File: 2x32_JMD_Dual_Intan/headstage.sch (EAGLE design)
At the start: 34 parts, among them U1 RHD2132_QFN, U2 RHD2132_QFN, U3 RHD2132_QFN

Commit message: Finished schematic of 64 chan JMD headstage, started layout.
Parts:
- removed C_A: 0.1uF, resistor:C-USC0402K
- removed C_A1, C_X1, C_Y1, C_Z1: 0.1uF, puggleboard:C_0402
- removed C_REF: 10nF, resistor:C-USC0402K
- removed C_REF1, C_REF2: 10nF, puggleboard:C_0402
- removed C_VDD: 10uF, resistor:C-USC0402K
- removed C_VDD1, C_VDD2: 10uF, puggleboard:C_0603
- removed LED: (no value), resistor:R-EU_R0402
- removed R5, R6: 100, resistor:R-EU_R0402
- removed RLED: 300, resistor:R-EU_R0402
- removed RLED1: 300, puggleboard:R_0402
- removed S2, S4: RHD2000-CABLE-AMP-SIDE, RHD2000:RHD2000-CABLE-AMP-SIDE
- removed S3: OMNETICS_A79025, RHD2000:OMNETICS_A79025
- removed U$2: ADXL335, voigts:ADXL335
- removed U3: RHD2132_QFN, RHD2000:RHD2132_QFN
- added AIN: PINHD-2X35_JMD70, puggleboard:PINHD-2X35_JMD70
- added C1: 0.1uF, puggleboard:C_0402
- added C2, C4: 10nF, puggleboard:C_0402
- added C3, C5: 10uF, puggleboard:C_0603
- C_X, C_Y, C_Z: device resistor:C-USC0402K -> puggleboard:C_0402
- JP1: value (none) -> PINHX-1X5; device puggleboard:PINHD-1X3 -> puggleboard:PINHX-1X5
- R1, R2, R3: device resistor:R-EU_R0402 -> puggleboard:R_0402
- R4: value 100 -> 300; device resistor:R-EU_R0402 -> puggleboard:R_0402
- S1: value OMNETICS_A79025 -> RHD2000-CABLE-AMP-SIDE; device RHD2000:OMNETICS_A79025 -> RHD2000:RHD2000-CABLE-AMP-SIDE
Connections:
- removed net ADC_REF: C_REF.1, U1.ADC_REF
- removed net AUX0UT_B: U3.AUXOUT
- removed net CS+: R1.2, S2.!CS!+, U1.!CS!+
- removed net CS-: R1.1, S2.!CS!-, U1.!CS!-
- removed net LEDOUT: LED.1, RLED.2
- removed net MISO1+: S2.MISO1+, U1.MISO+
- removed net MISO1-: S2.MISO1-, U1.MISO-
- removed net MOSI+: R3.2, S2.MOSI+, U1.MOSI+
- removed net MOSI-: R3.1, S2.MOSI-, U1.MOSI-
- removed net SCLK+: R2.2, S2.SCLK+, U1.SCLK+
- removed net SCLK-: R2.1, S2.SCLK-, U1.SCLK-
- removed net XOUT: C_X.2, U$1.XOUT, U1.AUXIN1
- removed net YOUT: C_Y.2, U$1.YOUT, U1.AUXIN2
- removed net ZOUT: C_Z.2, U$1.ZOUT, U1.AUXIN3
- new net AUXOUT_B: JP1.5, U2.AUXOUT
- new net N$3: C4.1, U2.ADC_REF
- new net N$7: C2.1, U1.ADC_REF
- net AUXOUT_A: now also JP1.4; no longer U2.AUXOUT
- net CS+1: now also R1.2, S1.!CS!+, U1.!CS!+; no longer R4.2, S4.!CS!+, U3.!CS!+
- net CS-1: now also R1.1, S1.!CS!-, U1.!CS!-; no longer R4.1, S4.!CS!-, U3.!CS!-
- net GND: now also C1.2, C2.2, C3.1, C4.2, C5.1, R4.1, S1.VDD; no longer C_A.2, C_A1.2, C_REF.2, C_REF1.1, C_REF1.2, C_REF2.1, C_REF2.2, C_VDD.1, C_VDD1.1, C_VDD2.1, C_X1.1, C_Y1.1, C_Z1.1, RLED.1, RLED1.1, S1.B1, S1.T18, S2.GND, S3.B1, S3.T18, S4.VDD, U$2.COM1, U$2.COM2, U$2.COM3, U$2.COM4, U$2.ST, U2.ADC_REF, U3.ADC_REF, U3.CTR, U3.ELEC_TEST, U3.GND1, U3.GND2, U3.GND3, U3.GND4, U3.VESD
- net IN0: now also AIN.3; no longer S1.B10, S3.B10, U2.IN0
- net IN1: now also AIN.4; no longer S1.B7, S3.B7, U2.IN1
- net IN10: now also AIN.13; no longer S1.T4, S3.T4, U2.IN10
- net IN11: now also AIN.14; no longer S1.T5, S3.T5, U2.IN11
- net IN12: now also AIN.15; no longer S1.T6, S3.T6, U2.IN12
- net IN13: now also AIN.16; no longer S1.T7, S3.T7, U2.IN13
- net IN14: now also AIN.17; no longer S1.T8, S3.T8, U2.IN14
- net IN15: now also AIN.18; no longer S1.T9, S3.T9, U2.IN15
- net IN16: now also AIN.19; no longer S1.T10, S3.T10, U2.IN16
- net IN17: now also AIN.20; no longer S1.T11, S3.T11, U2.IN17
- net IN18: now also AIN.21; no longer S1.T12, S3.T12, U2.IN18
- net IN19: now also AIN.22; no longer S1.T13, S3.T13, U2.IN19
- net IN2: now also AIN.5; no longer S1.B8, S3.B8, U2.IN2
- net IN20: now also AIN.23; no longer S1.T14, S3.T14, U2.IN20
- net IN21: now also AIN.24; no longer S1.T15, S3.T15, U2.IN21
- net IN22: now also AIN.25; no longer S1.T16, S3.T16, U2.IN22
- net IN23: now also AIN.26; no longer S1.T17, S3.T17, U2.IN23
- net IN24: now also AIN.27; no longer S1.B16, S3.B16, U2.IN24
- net IN25: now also AIN.28; no longer S1.B17, S3.B17, U2.IN25
- net IN26: now also AIN.29; no longer S1.B15, S3.B15, U2.IN26
- net IN27: now also AIN.30; no longer S1.B14, S3.B14, U2.IN27
- net IN28: now also AIN.31; no longer S1.B13, S3.B13, U2.IN28
- net IN29: now also AIN.32; no longer S1.B12, S3.B12, U2.IN29
- net IN3: now also AIN.6; no longer S1.B5, S3.B5, U2.IN3
- net IN30: now also AIN.33; no longer S1.B11, S3.B11, U2.IN30
- net IN31: now also AIN.34; no longer S1.B9, S3.B9, U2.IN31
- net IN32: now also AIN.37, U2.IN0; no longer U3.IN0
- net IN33: now also AIN.38, U2.IN1; no longer U3.IN1
- net IN34: now also AIN.39, U2.IN2; no longer U3.IN2
- net IN35: now also AIN.40, U2.IN3; no longer U3.IN3
- net IN36: now also AIN.41, U2.IN4; no longer U3.IN4
- net IN37: now also AIN.42, U2.IN5; no longer U3.IN5
- net IN38: now also AIN.43, U2.IN6; no longer U3.IN6
- net IN39: now also AIN.44, U2.IN7; no longer U3.IN7
- net IN4: now also AIN.7; no longer S1.B6, S3.B6, U2.IN4
- net IN40: now also AIN.45, U2.IN8; no longer U3.IN8
- net IN41: now also AIN.46, U2.IN9; no longer U3.IN9
- net IN42: now also AIN.47, U2.IN10; no longer U3.IN10
- net IN43: now also AIN.48, U2.IN11; no longer U3.IN11
- net IN44: now also AIN.49, U2.IN12; no longer U3.IN12
- net IN45: now also AIN.50, U2.IN13; no longer U3.IN13
- net IN46: now also AIN.51, U2.IN14; no longer U3.IN14
- net IN47: now also AIN.52, U2.IN15; no longer U3.IN15
- net IN48: now also AIN.53, U2.IN16; no longer U3.IN16
- net IN49: now also AIN.54, U2.IN17; no longer U3.IN17
- net IN5: now also AIN.8; no longer S1.B3, S3.B3, U2.IN5
- net IN50: now also AIN.55, U2.IN18; no longer U3.IN18
- net IN51: now also AIN.56, U2.IN19; no longer U3.IN19
- net IN52: now also AIN.57, U2.IN20; no longer U3.IN20
- net IN53: now also AIN.58, U2.IN21; no longer U3.IN21
- net IN54: now also AIN.59, U2.IN22; no longer U3.IN22
- net IN55: now also AIN.60, U2.IN23; no longer U3.IN23
- net IN56: now also AIN.61, U2.IN24; no longer U3.IN24
- net IN57: now also AIN.62, U2.IN25; no longer U3.IN25
- net IN58: now also AIN.63, U2.IN26; no longer U3.IN26
- net IN59: now also AIN.64, U2.IN27; no longer U3.IN27
- net IN6: now also AIN.9; no longer S1.B4, S3.B4, U2.IN6
- net IN60: now also AIN.65, U2.IN28; no longer U3.IN28
- net IN61: now also AIN.66, U2.IN29; no longer U3.IN29
- net IN62: now also AIN.67, U2.IN30; no longer U3.IN30
- net IN63: now also AIN.68, U2.IN31; no longer U3.IN31
- net IN7: now also AIN.10; no longer S1.B2, S3.B2, U2.IN7
- net IN8: now also AIN.11; no longer S1.T2, S3.T2, U2.IN8
- net IN9: now also AIN.12; no longer S1.T3, S3.T3, U2.IN9
- net LEDOUT1: now also R4.2; no longer RLED1.2
- net MISO1+1: now also S1.MISO1+, U1.MISO+; no longer S4.MISO1+, U2.MISO+
- net MISO1-1: now also S1.MISO1-, U1.MISO-; no longer S4.MISO1-, U2.MISO-
- net MOSI+1: now also R3.2, S1.MOSI+, U1.MOSI+; no longer R6.2, S4.MOSI+, U3.MOSI+
- net MOSI-1: now also R3.1, S1.MOSI-, U1.MOSI-; no longer R6.1, S4.MOSI-, U3.MOSI-
- net N$1: now also S1.MISO2-, U2.MISO-; no longer S4.MISO2-, U3.MISO-
- net N$2: now also S1.MISO2+, U2.MISO+; no longer S4.MISO2+, U3.MISO+
- net N$4: now also U2.AUXIN1; no longer U3.AUXIN1
- net N$5: now also U2.AUXIN2; no longer U3.AUXIN2
- net N$6: now also U2.AUXIN3; no longer U3.AUXIN3
- net REF: no longer S1.B18, S1.T1, S3.B18, S3.T1, U3.REF_ELEC
- net SCLK+1: now also R2.2, S1.SCLK+, U1.SCLK+; no longer R5.2, S4.SCLK+, U3.SCLK+
- net SCLK-1: now also R2.1, S1.SCLK-, U1.SCLK-; no longer R5.1, S4.SCLK-, U3.SCLK-
- net VDD: now also C1.1, C3.2, C5.2, S1.GND; no longer C_A.1, C_A1.1, C_VDD.2, C_VDD1.2, C_VDD2.2, LED.2, S2.VDD, S4.GND, U$2.VS1, U$2.VS2, U3.LVDS_EN, U3.VDD1, U3.VDD2, U3.VDD3
- net XOUT1: now also C_X.2, U$1.XOUT, U1.AUXIN1; no longer C_X1.2, U$2.XOUT, U2.AUXIN1
- net YOUT1: now also C_Y.2, U$1.YOUT, U1.AUXIN2; no longer C_Y1.2, U$2.YOUT, U2.AUXIN2
- net ZOUT1: now also C_Z.2, U$1.ZOUT, U1.AUXIN3; no longer C_Z1.2, U$2.ZOUT, U2.AUXIN3

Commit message: Minor.
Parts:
- JP1: value PINHX-1X5 -> PINHX-1X6; device puggleboard:PINHX-1X5 -> puggleboard:PINHX-1X6
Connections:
- net GND: now also JP1.6
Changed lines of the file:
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@@
 <part name="VDD17" library="supply1" deviceset="VDD" device=""/>
 <part name="PWR" library="puggleboard" deviceset="LED" device="_0603"/>
-<part name="JP1" library="puggleboard" deviceset="PINHX-1X5" device=""/>
+<part name="JP1" library="puggleboard" deviceset="PINHX-1X6" device=""/>
 <part name="AIN" library="puggleboard" deviceset="PINHD-2X35" device="_JMD70"/>
 </parts>
@@
 <pinref part="U2" gate="A" pin="GND3"/>
 <pinref part="GND32" gate="1" pin="GND"/>
-<wire x1="231.14" y1="129.54" x2="231.14" y2="119.38" width="0.1524" layer="91"/>
+<wire x1="231.14" y1="129.54" x2="231.14" y2="121.92" width="0.1524" layer="91"/>
+<pinref part="JP1" gate="G$1" pin="6"/>
+<wire x1="231.14" y1="121.92" x2="231.14" y2="119.38" width="0.1524" layer="91"/>
+<wire x1="231.14" y1="121.92" x2="223.52" y2="121.92" width="0.1524" layer="91"/>
+<wire x1="223.52" y1="121.92" x2="223.52" y2="104.14" width="0.1524" layer="91"/>
+<junction x="231.14" y="121.92"/>
 </segment>
 </net>

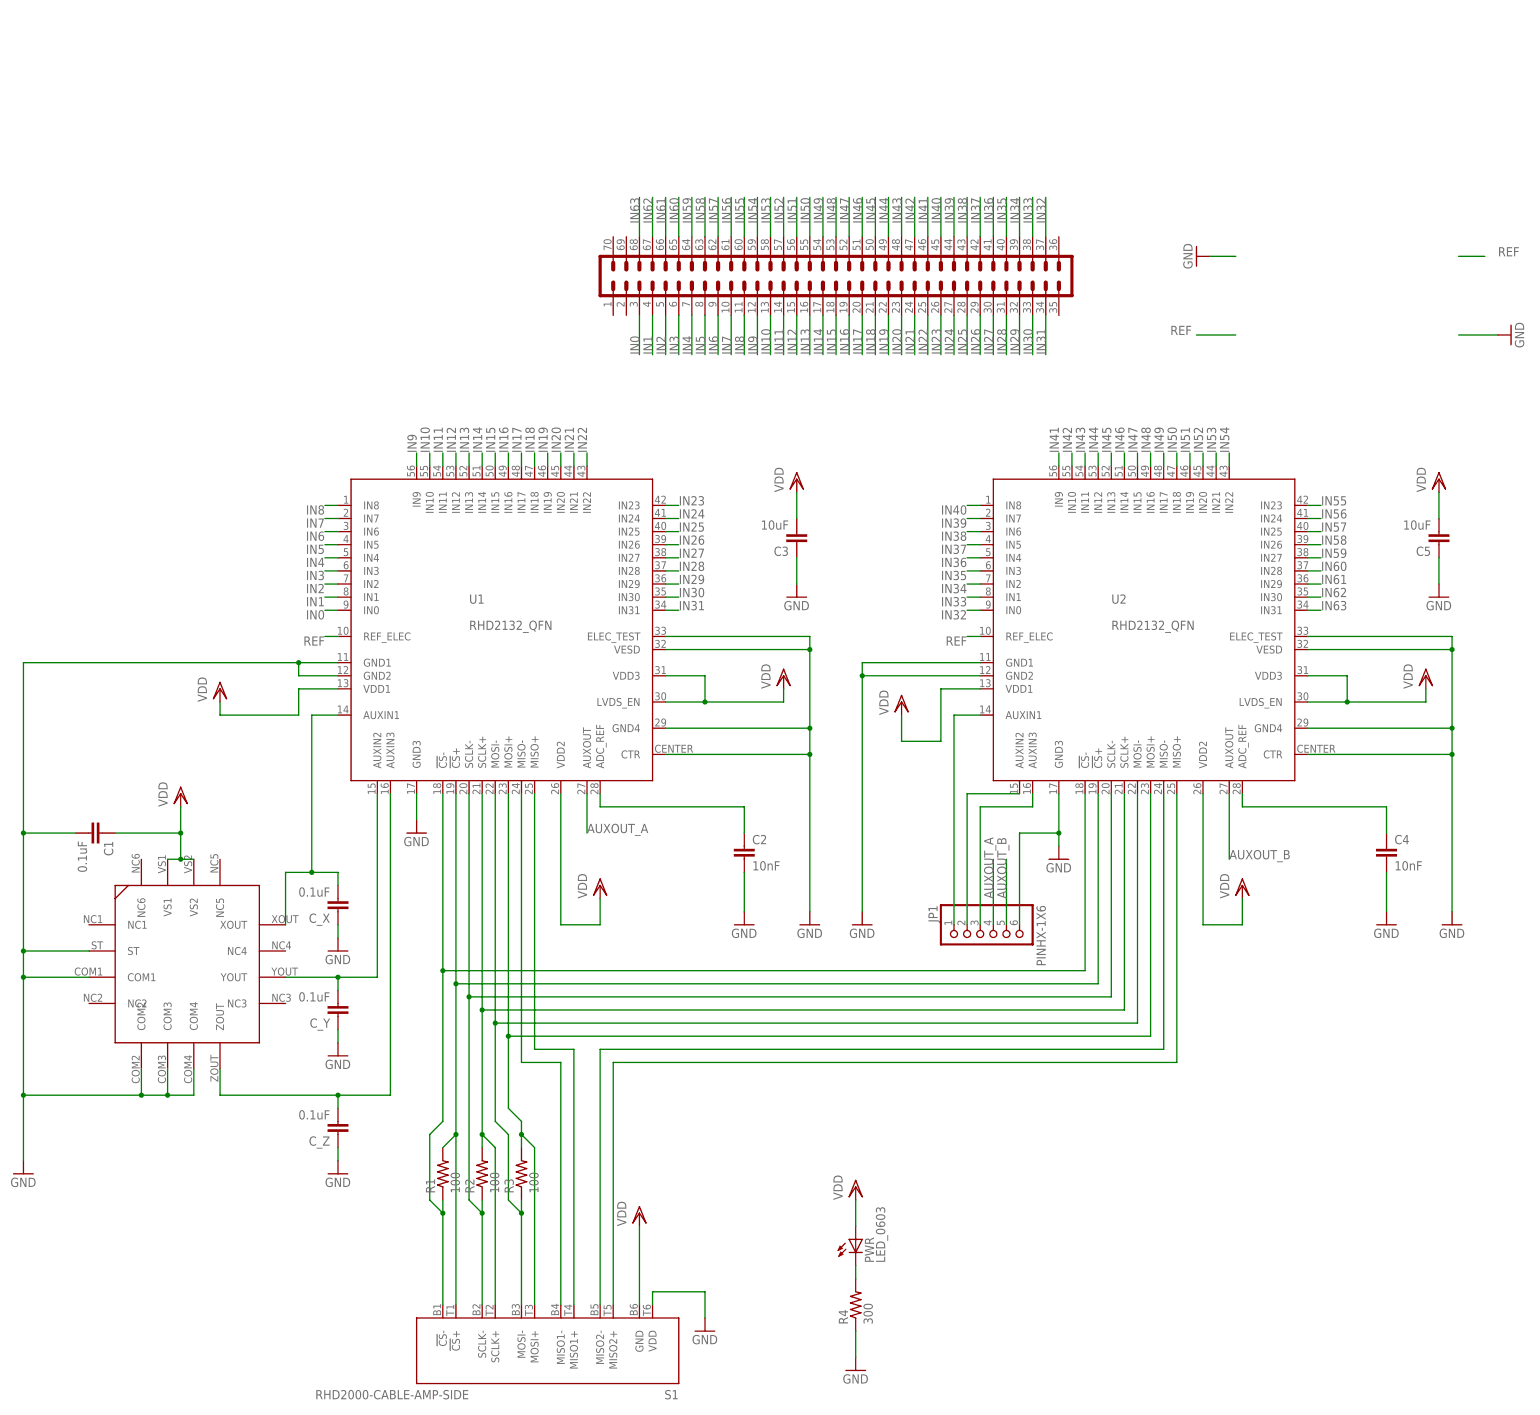
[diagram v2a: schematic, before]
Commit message: Finished initial layout for the 64 channel headstage. I will also make cable interface board. This will be an optional component useful for linking two 64 channel headstages to get 128 with head tracking etc.
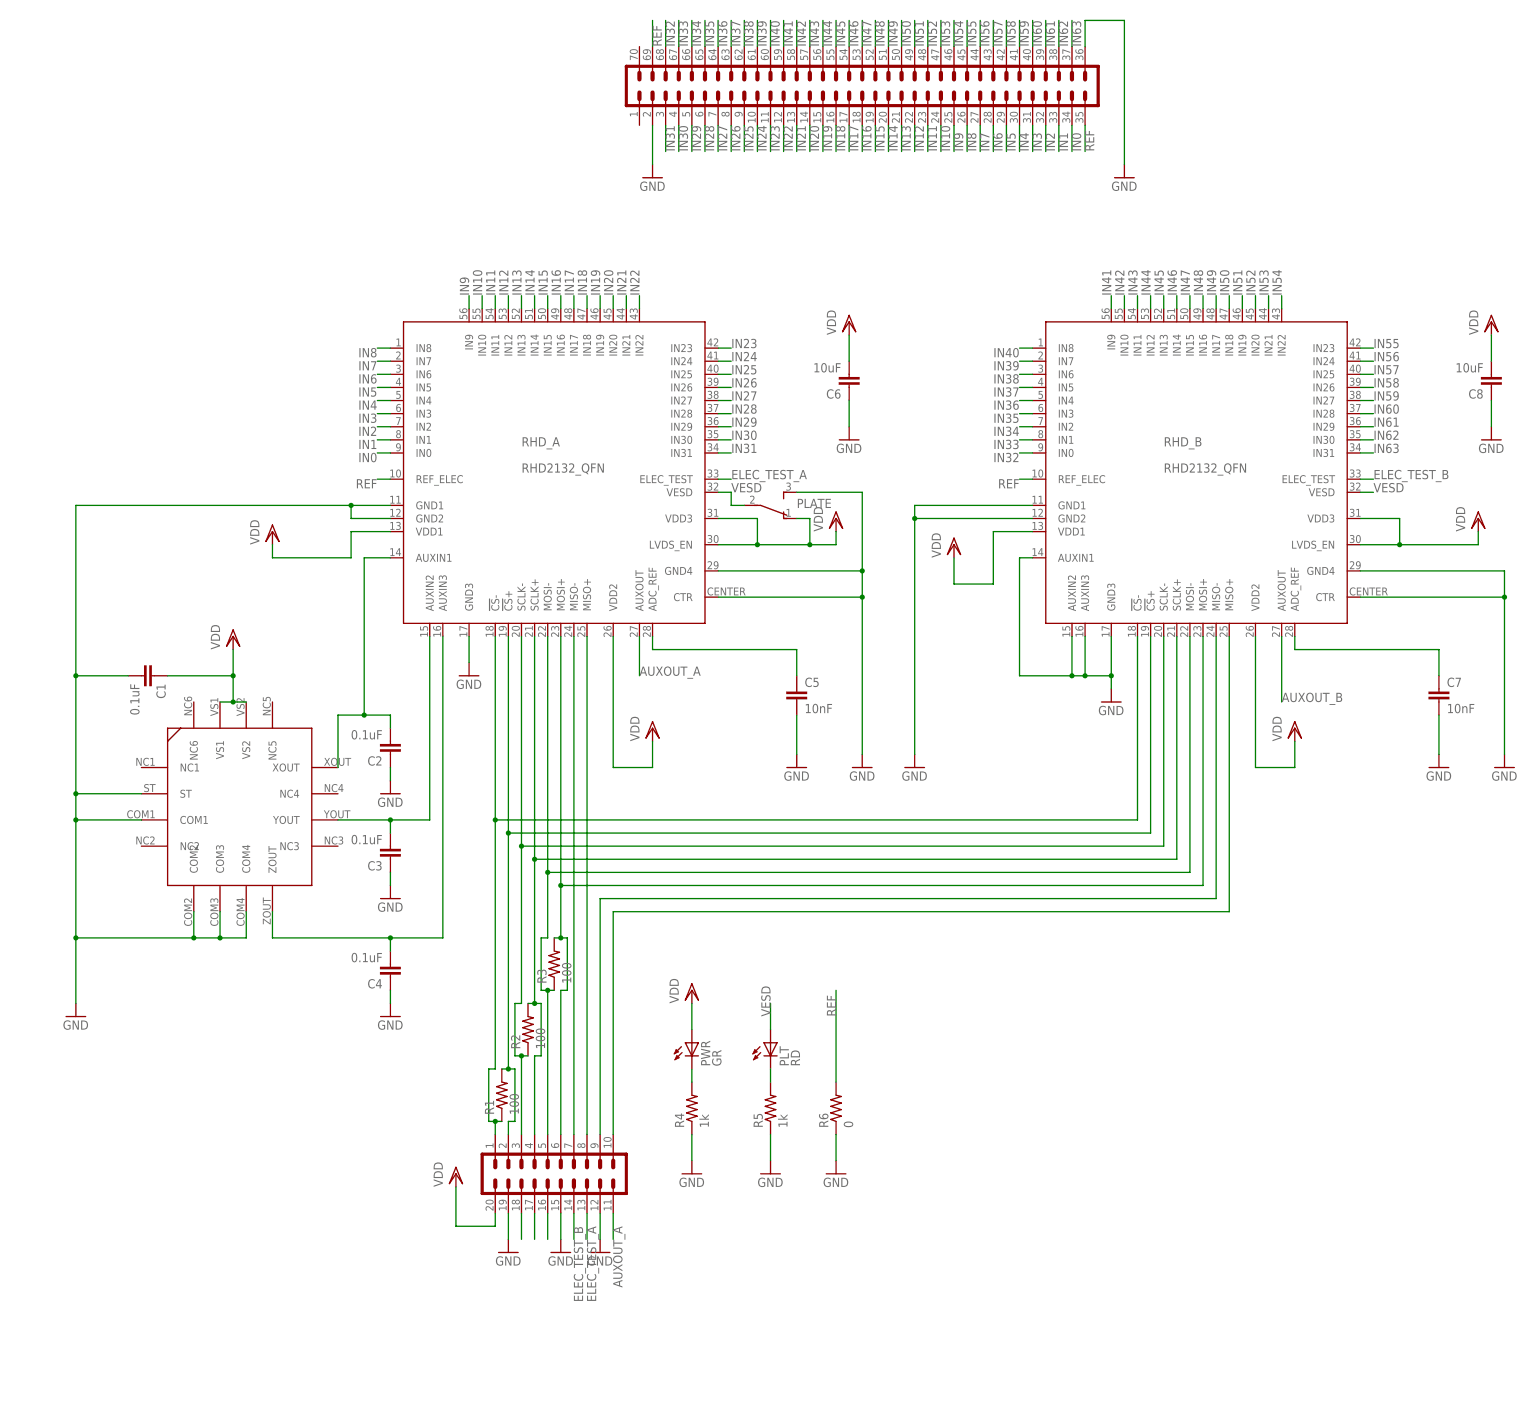
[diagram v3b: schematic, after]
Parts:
- removed C_X, C_Y, C_Z: 0.1uF, puggleboard:C_0402
- removed JP1: PINHX-1X6, puggleboard:PINHX-1X6
- removed S1: RHD2000-CABLE-AMP-SIDE, RHD2000:RHD2000-CABLE-AMP-SIDE
- removed U1, U2: RHD2132_QFN, RHD2000:RHD2132_QFN
- added C6, C8: 10uF, headstage:C_0603
- added C7: 10nF, headstage:C_0402
- added OUT: JMD, headstage:PINHD-2X10_JMD
- added PLATE: (no value), headstage:SPDT_PCM12
- added PLT: RD, puggleboard:LED_0603
- added R5: 1k, headstage:R_0402
- added R6: 0, headstage:R_0402
- added RHD_A, RHD_B: RHD2132_QFN, headstage:RHD2132_QFN
- AIN: value PINHD-2X35_JMD70 -> JMD70; device puggleboard:PINHD-2X35_JMD70 -> headstage:PINHD-2X35_JMD70
- C1: device puggleboard:C_0402 -> headstage:C_0402
- C2, C4: value 10nF -> 0.1uF; device puggleboard:C_0402 -> headstage:C_0402
- C3: value 10uF -> 0.1uF; device puggleboard:C_0603 -> headstage:C_0402
- C5: value 10uF -> 10nF; device puggleboard:C_0603 -> headstage:C_0402
- PWR: value LED_0603 -> GR
- R1, R2, R3: device puggleboard:R_0402 -> headstage:R_0402
- R4: value 300 -> 1k; device puggleboard:R_0402 -> headstage:R_0402
- U$1: device voigts:ADXL335 -> headstage:ADXL335
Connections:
- removed net CS+1: R1.2, S1.!CS!+, U1.!CS!+, U2.!CS!+
- removed net CS-1: R1.1, S1.!CS!-, U1.!CS!-, U2.!CS!-
- removed net MISO1+1: S1.MISO1+, U1.MISO+
- removed net MISO1-1: S1.MISO1-, U1.MISO-
- removed net MOSI+1: R3.2, S1.MOSI+, U1.MOSI+, U2.MOSI+
- removed net MOSI-1: R3.1, S1.MOSI-, U1.MOSI-, U2.MOSI-
- removed net N$1: S1.MISO2-, U2.MISO-
- removed net N$2: S1.MISO2+, U2.MISO+
- removed net N$4: JP1.1, U2.AUXIN1
- removed net N$5: JP1.2, U2.AUXIN2
- removed net N$6: JP1.3, U2.AUXIN3
- removed net SCLK+1: R2.2, S1.SCLK+, U1.SCLK+, U2.SCLK+
- removed net SCLK-1: R2.1, S1.SCLK-, U1.SCLK-, U2.SCLK-
- new net CS+: OUT.2, R1.2, RHD_A.!CS!+, RHD_B.!CS!+
- new net CS-: OUT.1, R1.1, RHD_A.!CS!-, RHD_B.!CS!-
- new net ELEC_TEST_A: OUT.13, RHD_A.ELEC_TEST
- new net ELEC_TEST_B: OUT.14, RHD_B.ELEC_TEST
- new net LEDOUT2: PLT.C, R5.2
- new net MIS02-: OUT.9, RHD_B.MISO-
- new net MISO1+: OUT.8, RHD_A.MISO+
- new net MISO1-: OUT.7, RHD_A.MISO-
- new net MISO2+: OUT.10, RHD_B.MISO+
- new net MOSI+: OUT.6, R3.2, RHD_A.MOSI+, RHD_B.MOSI+
- new net MOSI-: OUT.5, R3.1, RHD_A.MOSI-, RHD_B.MOSI-
- new net N$10: OUT.16
- new net N$8: OUT.18
- new net N$9: OUT.17
- new net SCLK+: OUT.4, R2.2, RHD_A.SCLK+, RHD_B.SCLK+
- new net SCLK-: OUT.3, R2.1, RHD_A.SCLK-, RHD_B.SCLK-
- new net VESD: PLATE.2, PLT.A, RHD_A.VESD, RHD_B.VESD
- net AUXOUT_A: now also OUT.11, RHD_A.AUXOUT; no longer JP1.4, U1.AUXOUT
- net AUXOUT_B: now also RHD_B.AUXOUT; no longer JP1.5, U2.AUXOUT
- net GND: now also AIN.2, AIN.36, C2.1, C4.1, C5.2, C6.1, C7.2, C8.1, OUT.12, OUT.15, OUT.19, PLATE.3, R5.1, R6.1, RHD_A.CTR, RHD_A.GND1, RHD_A.GND2, RHD_A.GND3, RHD_A.GND4, RHD_B.AUXIN1, RHD_B.AUXIN2, RHD_B.AUXIN3, RHD_B.CTR, RHD_B.GND1, RHD_B.GND2, RHD_B.GND3, RHD_B.GND4; no longer C2.2, C4.2, C5.1, C_X.1, C_Y.1, C_Z.1, JP1.6, S1.VDD, U1.CTR, U1.ELEC_TEST, U1.GND1, U1.GND2, U1.GND3, U1.GND4, U1.VESD, U2.CTR, U2.ELEC_TEST, U2.GND1, U2.GND2, U2.GND3, U2.GND4, U2.VESD
- net IN0: now also AIN.34, RHD_A.IN0; no longer AIN.3, U1.IN0
- net IN1: now also AIN.33, RHD_A.IN1; no longer AIN.4, U1.IN1
- net IN10: now also AIN.24, RHD_A.IN10; no longer AIN.13, U1.IN10
- net IN11: now also AIN.23, RHD_A.IN11; no longer AIN.14, U1.IN11
- net IN12: now also AIN.22, RHD_A.IN12; no longer AIN.15, U1.IN12
- net IN13: now also AIN.21, RHD_A.IN13; no longer AIN.16, U1.IN13
- net IN14: now also AIN.20, RHD_A.IN14; no longer AIN.17, U1.IN14
- net IN15: now also AIN.19, RHD_A.IN15; no longer AIN.18, U1.IN15
- net IN16: now also AIN.18, RHD_A.IN16; no longer AIN.19, U1.IN16
- net IN17: now also AIN.17, RHD_A.IN17; no longer AIN.20, U1.IN17
- net IN18: now also AIN.16, RHD_A.IN18; no longer AIN.21, U1.IN18
- net IN19: now also AIN.15, RHD_A.IN19; no longer AIN.22, U1.IN19
- net IN2: now also AIN.32, RHD_A.IN2; no longer AIN.5, U1.IN2
- net IN20: now also AIN.14, RHD_A.IN20; no longer AIN.23, U1.IN20
- net IN21: now also AIN.13, RHD_A.IN21; no longer AIN.24, U1.IN21
- net IN22: now also AIN.12, RHD_A.IN22; no longer AIN.25, U1.IN22
- net IN23: now also AIN.11, RHD_A.IN23; no longer AIN.26, U1.IN23
- net IN24: now also AIN.10, RHD_A.IN24; no longer AIN.27, U1.IN24
- net IN25: now also AIN.9, RHD_A.IN25; no longer AIN.28, U1.IN25
- net IN26: now also AIN.8, RHD_A.IN26; no longer AIN.29, U1.IN26
- net IN27: now also AIN.7, RHD_A.IN27; no longer AIN.30, U1.IN27
- net IN28: now also AIN.6, RHD_A.IN28; no longer AIN.31, U1.IN28
- net IN29: now also AIN.5, RHD_A.IN29; no longer AIN.32, U1.IN29
- net IN3: now also AIN.31, RHD_A.IN3; no longer AIN.6, U1.IN3
- net IN30: now also AIN.4, RHD_A.IN30; no longer AIN.33, U1.IN30
- net IN31: now also AIN.3, RHD_A.IN31; no longer AIN.34, U1.IN31
- net IN32: now also AIN.68, RHD_B.IN0; no longer AIN.37, U2.IN0
- net IN33: now also AIN.67, RHD_B.IN1; no longer AIN.38, U2.IN1
- net IN34: now also AIN.66, RHD_B.IN2; no longer AIN.39, U2.IN2
- net IN35: now also AIN.65, RHD_B.IN3; no longer AIN.40, U2.IN3
- net IN36: now also AIN.64, RHD_B.IN4; no longer AIN.41, U2.IN4
- net IN37: now also AIN.63, RHD_B.IN5; no longer AIN.42, U2.IN5
- net IN38: now also AIN.62, RHD_B.IN6; no longer AIN.43, U2.IN6
- net IN39: now also AIN.61, RHD_B.IN7; no longer AIN.44, U2.IN7
- net IN4: now also AIN.30, RHD_A.IN4; no longer AIN.7, U1.IN4
- net IN40: now also AIN.60, RHD_B.IN8; no longer AIN.45, U2.IN8
- net IN41: now also AIN.59, RHD_B.IN9; no longer AIN.46, U2.IN9
- net IN42: now also AIN.58, RHD_B.IN10; no longer AIN.47, U2.IN10
- net IN43: now also AIN.57, RHD_B.IN11; no longer AIN.48, U2.IN11
- net IN44: now also AIN.56, RHD_B.IN12; no longer AIN.49, U2.IN12
- net IN45: now also AIN.55, RHD_B.IN13; no longer AIN.50, U2.IN13
- net IN46: now also AIN.54, RHD_B.IN14; no longer AIN.51, U2.IN14
- net IN47: now also AIN.53, RHD_B.IN15; no longer AIN.52, U2.IN15
- net IN48: now also AIN.52, RHD_B.IN16; no longer AIN.53, U2.IN16
- net IN49: now also AIN.51, RHD_B.IN17; no longer AIN.54, U2.IN17
- net IN5: now also AIN.29, RHD_A.IN5; no longer AIN.8, U1.IN5
- net IN50: now also AIN.50, RHD_B.IN18; no longer AIN.55, U2.IN18
- net IN51: now also AIN.49, RHD_B.IN19; no longer AIN.56, U2.IN19
- net IN52: now also AIN.48, RHD_B.IN20; no longer AIN.57, U2.IN20
- net IN53: now also AIN.47, RHD_B.IN21; no longer AIN.58, U2.IN21
- net IN54: now also AIN.46, RHD_B.IN22; no longer AIN.59, U2.IN22
- net IN55: now also AIN.45, RHD_B.IN23; no longer AIN.60, U2.IN23
- net IN56: now also AIN.44, RHD_B.IN24; no longer AIN.61, U2.IN24
- net IN57: now also AIN.43, RHD_B.IN25; no longer AIN.62, U2.IN25
- net IN58: now also AIN.42, RHD_B.IN26; no longer AIN.63, U2.IN26
- net IN59: now also AIN.41, RHD_B.IN27; no longer AIN.64, U2.IN27
- net IN6: now also AIN.28, RHD_A.IN6; no longer AIN.9, U1.IN6
- net IN60: now also AIN.40, RHD_B.IN28; no longer AIN.65, U2.IN28
- net IN61: now also AIN.39, RHD_B.IN29; no longer AIN.66, U2.IN29
- net IN62: now also AIN.38, RHD_B.IN30; no longer AIN.67, U2.IN30
- net IN63: now also AIN.37, RHD_B.IN31; no longer AIN.68, U2.IN31
- net IN7: now also AIN.27, RHD_A.IN7; no longer AIN.10, U1.IN7
- net IN8: now also AIN.26, RHD_A.IN8; no longer AIN.11, U1.IN8
- net IN9: now also AIN.25, RHD_A.IN9; no longer AIN.12, U1.IN9
- net N$3: now also C7.1, RHD_B.ADC_REF; no longer C4.1, U2.ADC_REF
- net N$7: now also C5.1, RHD_A.ADC_REF; no longer C2.1, U1.ADC_REF
- net REF: now also AIN.35, AIN.69, R6.2, RHD_A.REF_ELEC, RHD_B.REF_ELEC; no longer U1.REF_ELEC, U2.REF_ELEC
- net VDD: now also C6.2, C8.2, OUT.20, PLATE.1, RHD_A.LVDS_EN, RHD_A.VDD1, RHD_A.VDD2, RHD_A.VDD3, RHD_B.LVDS_EN, RHD_B.VDD1, RHD_B.VDD2, RHD_B.VDD3; no longer C3.2, C5.2, S1.GND, U1.LVDS_EN, U1.VDD1, U1.VDD2, U1.VDD3, U2.LVDS_EN, U2.VDD1, U2.VDD2, U2.VDD3
- net XOUT1: now also C2.2, RHD_A.AUXIN1; no longer C_X.2, U1.AUXIN1
- net YOUT1: now also C3.2, RHD_A.AUXIN2; no longer C_Y.2, U1.AUXIN2
- net ZOUT1: now also C4.2, RHD_A.AUXIN3; no longer C_Z.2, U1.AUXIN3
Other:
- moved on the sheet: C1, C2, C3, C4, C5, PWR, R1, R2, R3, R4
